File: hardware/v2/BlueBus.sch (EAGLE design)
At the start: 134 parts, among them J1 3PIN_953442_1, J2 6PIN_953442_1, J3 6PIN_5_103166_1, J4 SJ2-35853A-SMT-TR, J5 SMB_CONN, J6 USB3080-30-01-A, J7 PCM12SMTR, J8 TC2030, Q1 NMOSFET-BSS138K, Q2 PMOSFET-DMP32D4SSOT323, Q3 NMOSFET-BSS138K, U1 MPQ4420, U10 PCM5122, U11 PAM8406, U2 TH3122.4, U3 FT231XS, U4 S-1212BC0-U5T1U, U5 XC6210, U6 CAT25M01, U7 PIC24FJ1024GA606, U8 BM83SM1, U9 DIT4096

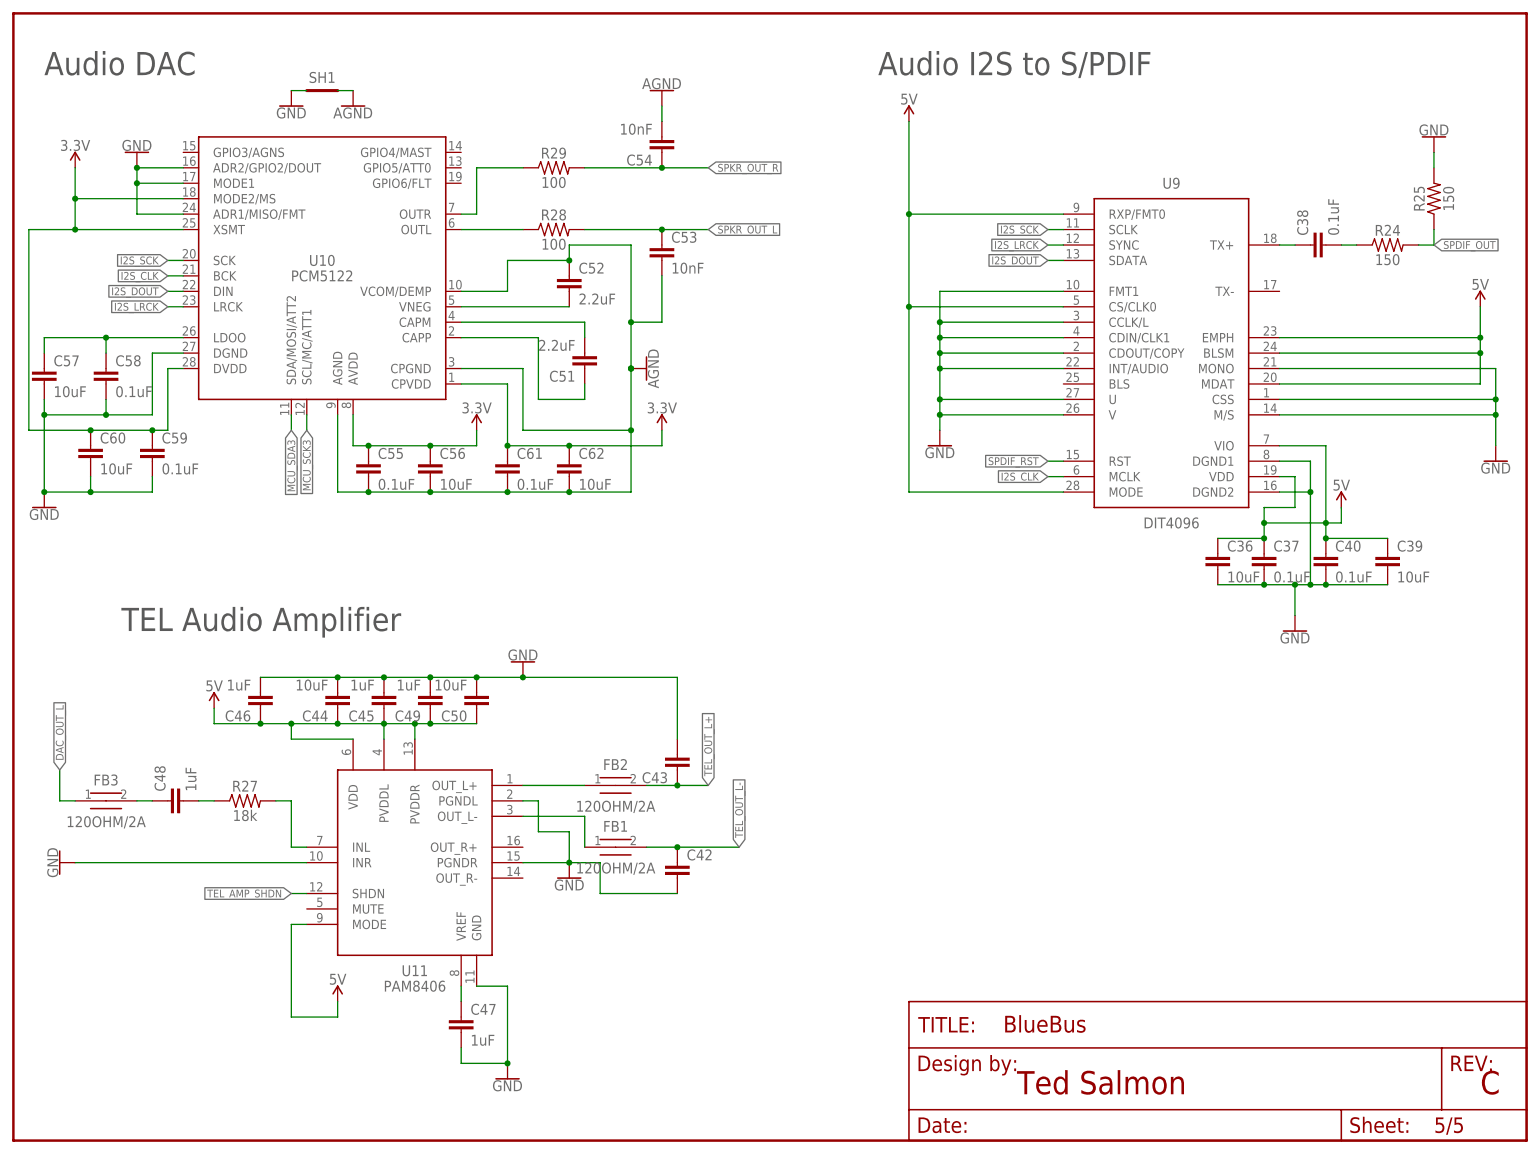
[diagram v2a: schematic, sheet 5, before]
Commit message: [IMP] hardware: V2 Bugfixes and improvements Bug fixes:     * Wire floating S/PDIF reset pin to MCU     * Add pull up to MCU pin 64 for board identification Improvements:     * Added a 0.3mm isolation of the ground plane     * Switched by design rules to metric     * Moved the pin 1 indicators out from under the ICs to the side of pin 1     * Added outlines for all passives     * Moved over the impedance circuit for the S/PDIF output and kept the trace on the top layer     * Moved more traces off the bottom layer     * Moved the I2S lines to the top layer and reduced the VIA count from 11 to 5     * Revised all the packages in the design to ensure they matched the D/S. Specifically, the PIC24s package now has 0.3mm pads     * Set the minimum trace size to 0.25mm instead of 0.20mm     * Added more VIA floods for the ground plane to tie them together where the bottom layer gets bifurcated
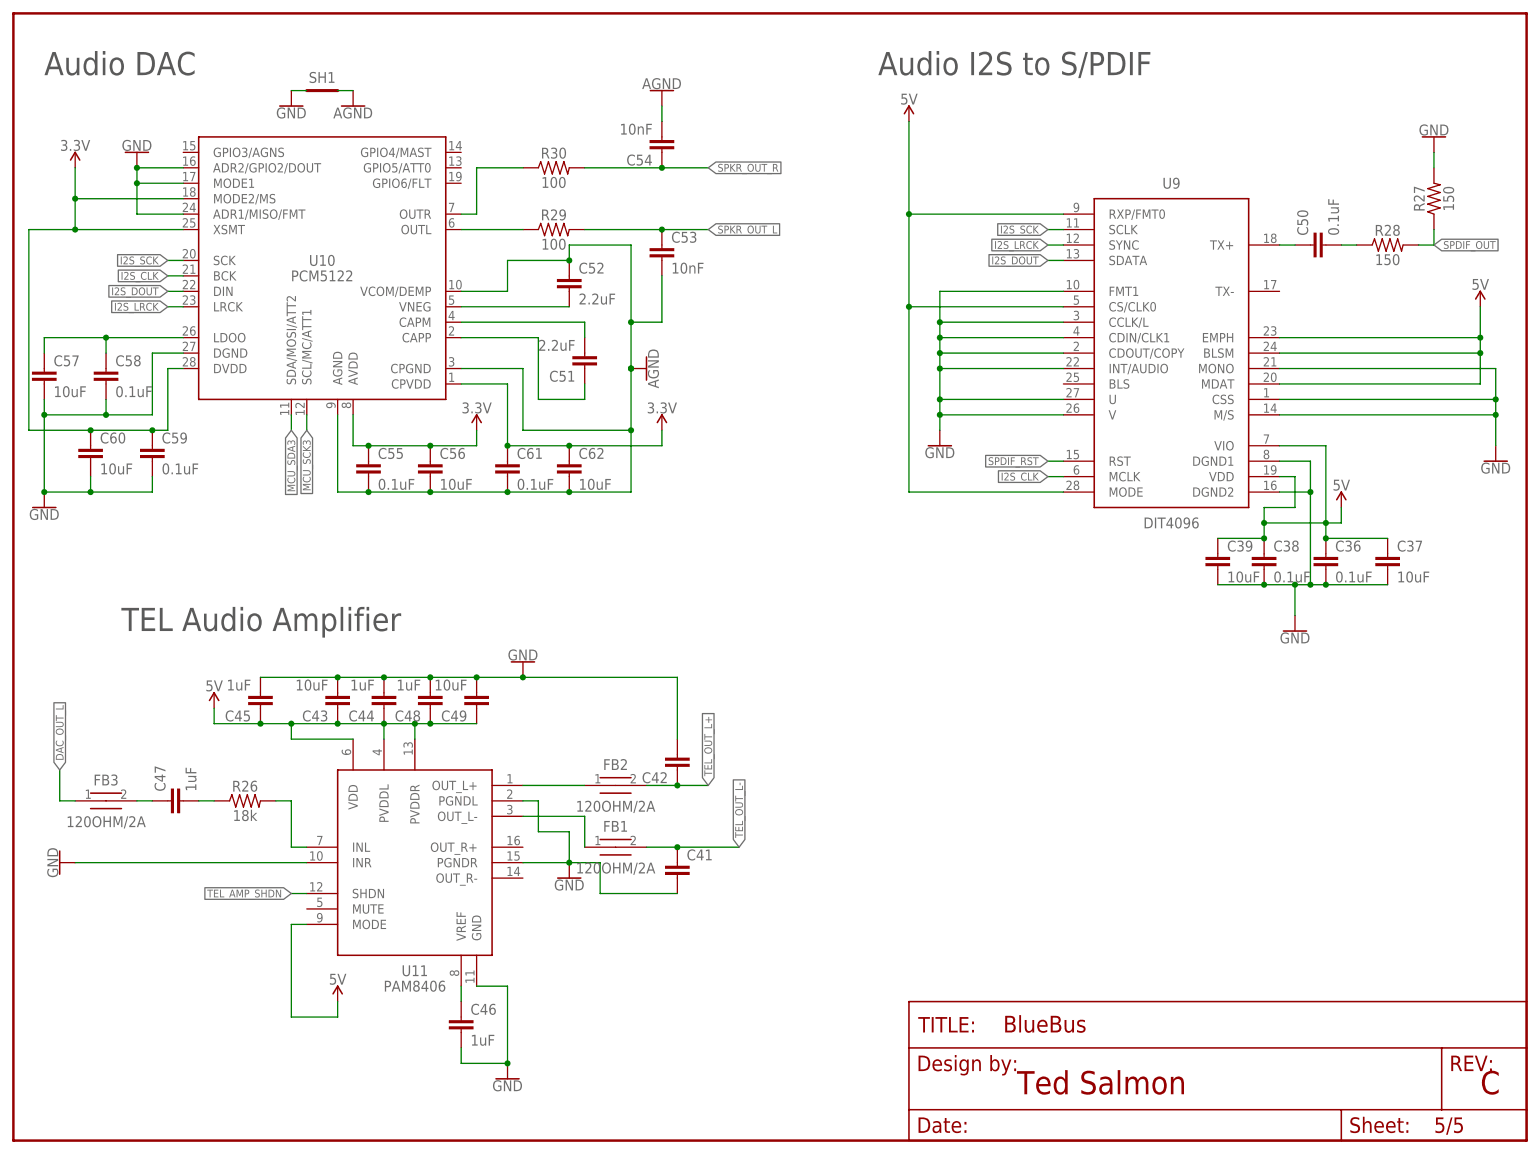
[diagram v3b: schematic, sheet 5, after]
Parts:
- added R30: 100, Passives:100OHM0603
- C31, C32: value 47nF -> 1uF; device Passives:47NF0603 -> Passives:1UF0603
- C33: value 200pF -> 47nF; device Passives:220PF0603 -> Passives:47NF0603
- C34: value 1uF -> 200pF; device Passives:1UF0603 -> Passives:220PF0603
- C35: value 1uF -> 47nF; device Passives:1UF0603 -> Passives:47NF0603
- C36, C50: value 10uF -> 0.1uF; device Passives:10UF0603 -> Passives:0.1UF0603
- C37: value 0.1uF -> 10uF; device Passives:0.1UF0603 -> Passives:10UF0603
- C40: value 0.1uF -> 47UF1206; device Passives:0.1UF0603 -> Passives:47UF1206
- C41: value 47UF1206 -> 200pF; device Passives:47UF1206 -> Passives:220PF0603
- C43: value 200pF -> 10uF; device Passives:220PF0603 -> Passives:10UF0603
- C44: value 10uF -> 1uF; device Passives:10UF0603 -> Passives:1UF0603
- C49: value 1uF -> 10uF; device Passives:1UF0603 -> Passives:10UF0603
- R10: value 20 -> 100k; device Passives:20OHM0603 -> Passives:100KOHM0603
- R17: value 20 -> 10k; device Passives:20OHM0603 -> Passives:10KOHM0603
- R19: value 2k -> 20; device Passives:2KOHM0603 -> Passives:20OHM0603
- R22: value 1k -> 2k; device Passives:1KOHM0603 -> Passives:2KOHM0603
- R24: value 150 -> 1k; device Passives:150OHM0603 -> Passives:1KOHM0603
- R25: value 150 -> 10k; device Passives:150OHM0603 -> Passives:10KOHM0603
- R26: value 10k -> 18k; device Passives:10KOHM0603 -> Passives:18KOHM0603
- R27: value 18k -> 150; device Passives:18KOHM0603 -> Passives:150OHM0603
- R28: value 100 -> 150; device Passives:100OHM0603 -> Passives:150OHM0603
- R5: value 100k -> 20; device Passives:100KOHM0603 -> Passives:20OHM0603
- R6: value 41.2k -> 100k; device Passives:41.2KOHM0603 -> Passives:100KOHM0603
- R7: value 7.68k -> 41.2k; device Passives:7.68KOHM0603 -> Passives:41.2KOHM0603
- R8: value 51k -> 7.68k; device Passives:51KOHM0603 -> Passives:7.68KOHM0603
- R9: value 100k -> 51k; device Passives:100KOHM0603 -> Passives:51KOHM0603
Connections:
- new net MCU_VER: R16.1, U7.HLVDIN/CTED8/PMD4/RE4
- net 12V: now also R25.1; no longer R26.1
- net 3.3V: now also R17.2
- net 5V: now also C38.1, C43.1, C48.1, R7.2; no longer C40.1, C46.1, C50.1, R6.2
- net 5VREG_BS: now also R5.1; no longer R10.1
- net 5VREG_BS_CAP: now also R5.2; no longer R10.2
- net 5VREG_EN: now also R6.1; no longer R5.1
- net 5VREG_FB: now also R9.2; no longer R8.2
- net 5VREG_FB_T: now also R7.1, R8.2, R9.1; no longer R6.1, R7.2, R8.1
- net 5VREG_PG: now also R10.1; no longer R9.1
- net 5VREG_VCC: now also R10.2; no longer R9.2
- net BT_MIC_L: now also C34.1, C40.1; no longer C32.1, C41.1
- net DAC_OUT_L: now also R29.1; no longer R28.1
- net DAC_OUT_R: now also R30.1; no longer R29.1
- net GND: now also C31.2, C32.2, C35.1, C38.2, C41.2, C48.2, R27.2, R8.1; no longer C31.1, C33.2, C35.2, C40.2, C47.2, C50.2, R25.2, R7.1
- net IBUS: now also R19.1; no longer R17.1
- net IBUS_5V: now also R6.2; no longer R5.2
- net IBUS_FILT: now also R19.2; no longer R17.2
- net MCU_ON_LED: now also R20.2; no longer R21.2
- net MCU_ON_LED_RES: now also R20.1; no longer R21.1
- net MCU_SCK3: now also R13.1; no longer R12.1
- net MCU_SDA3: now also R12.1; no longer R13.1
- net MICN1: now also C35.2; no longer C31.2
- net MICP1: now also C33.2; no longer C32.2
- net MICP1_RES: now also C31.1, R24.1; no longer C35.1, R22.1
- net MIC_BIAS: now also C32.1, R24.2; no longer C34.1, R22.2
- net RECOVERY_ON: now also R17.1; no longer R16.1
- net SPDIF_OUT: now also R27.1, R28.2; no longer R24.2, R25.1
- net SPDIF_RST: now also U7.PMD2/RE2
- net SPDIF_TX_FLT: now also C50.1; no longer C38.1
- net SPDIF_TX_RES: now also C50.2, R28.1; no longer C38.2, R24.1
- net SPKR_OUT_L: now also R29.2; no longer R28.2
- net SPKR_OUT_R: now also R30.2; no longer R29.2
- net SYS_RX_LED: now also R21.2; no longer R20.2
- net SYS_RX_LED_RES: now also R21.1; no longer R20.1
- net SYS_TX_LED: now also R22.2; no longer R19.2
- net SYS_TX_LED_RES: now also R22.1; no longer R19.1
- net TEL_AMP_IN: now also C47.1; no longer C48.1
- net TEL_AMP_INL: now also R26.2; no longer R27.2
- net TEL_AMP_INL_CAP_RES: now also C47.2, R26.1; no longer C48.2, R27.1
- net TEL_AMP_VREF: now also C46.1; no longer C47.1
- net TEL_MIC_L_OUT: now also C40.2, R25.2; no longer C41.2, R26.2
- net TEL_OUT_L+: now also C42.1; no longer C43.1
- net TEL_OUT_L-: now also C41.1; no longer C42.1
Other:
- moved on the sheet: C31, C32, C33, C34, C35, C36, C37, C38, C39, C42, C43, C44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

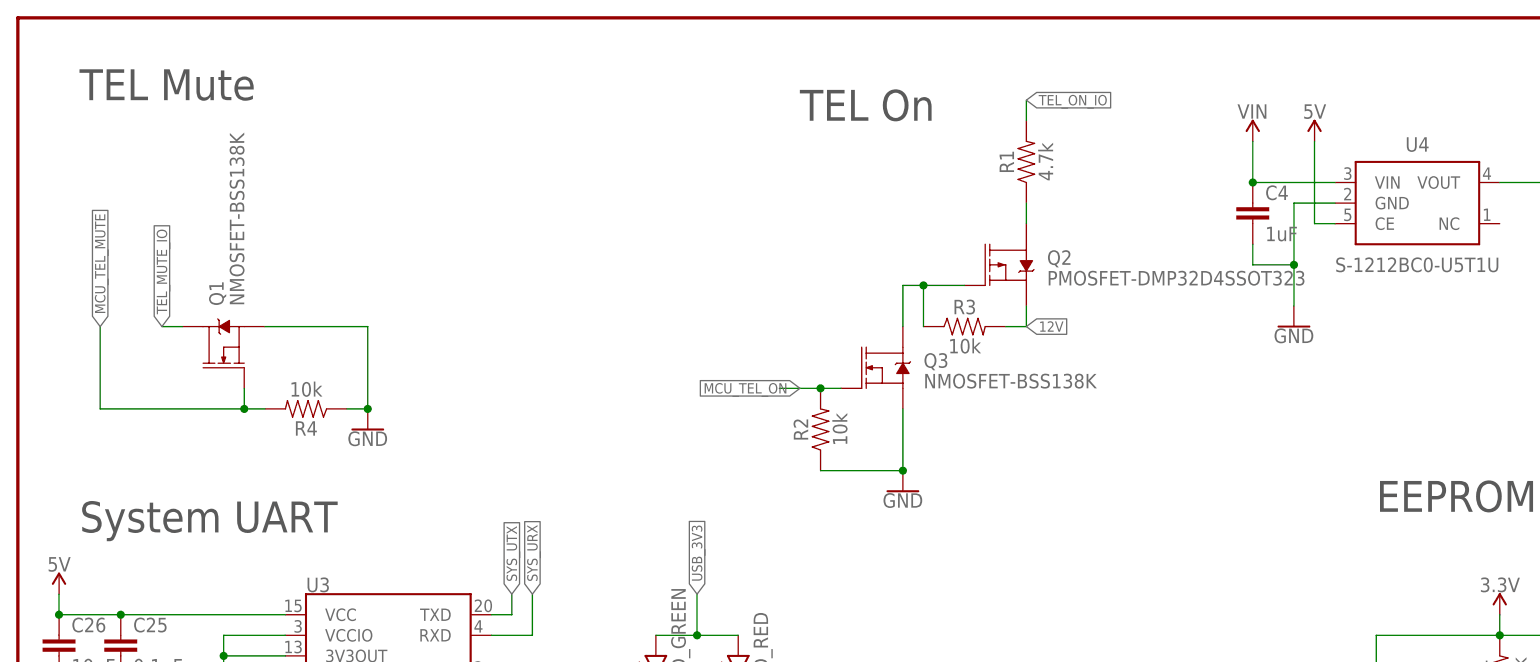
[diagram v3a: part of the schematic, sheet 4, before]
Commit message: [IMP] hardware: v2.0 TEL Circuit * Add Series resistor and move MOSFETs and resistors around to support BJT usage
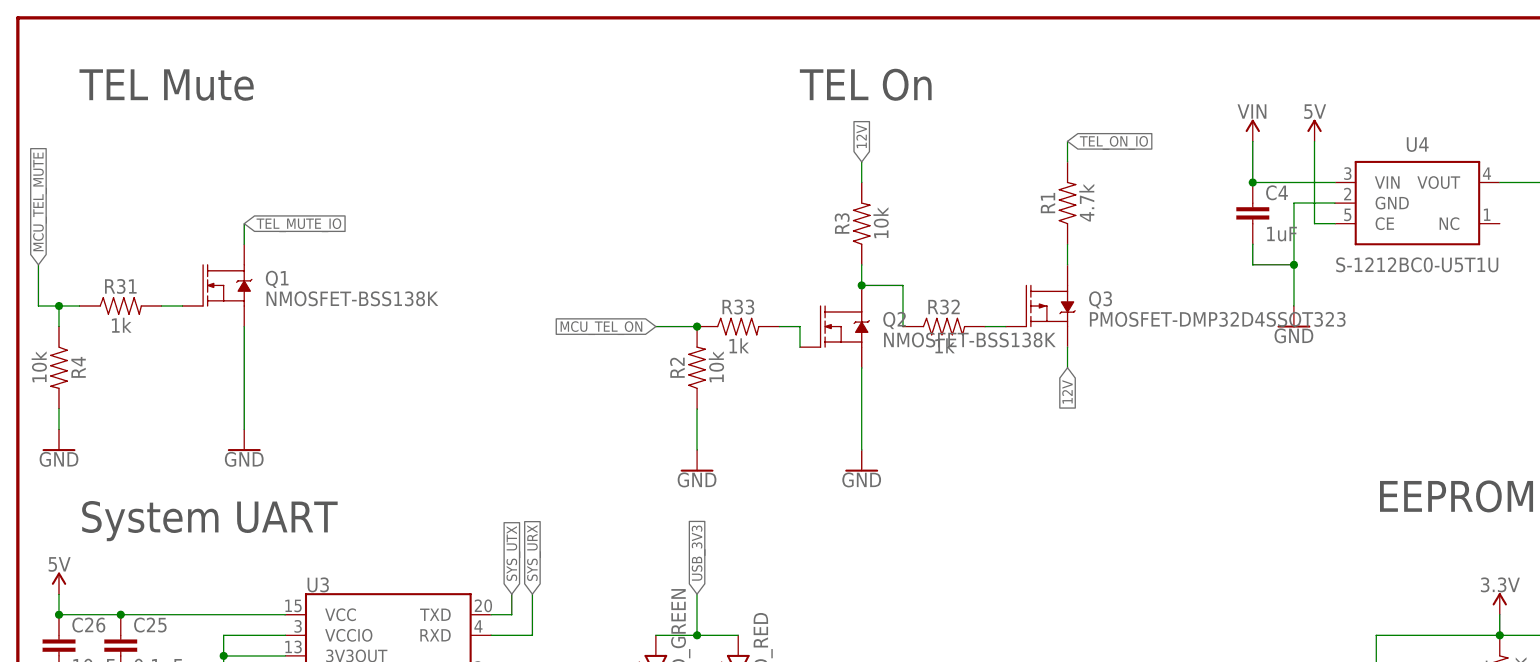
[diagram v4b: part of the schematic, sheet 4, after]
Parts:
- added D3: SMBJ18A, Passives:SMBJ18A
- added R31, R32, R33: 1k, Passives:1KOHM0603
- J8: value TC2030 -> TC2030NL; device Connectors:TC2030 -> Connectors:TC2030NL
- Q2: value PMOSFET-DMP32D4SSOT323 -> NMOSFET-BSS138K; device Passives:PMOSFET-DMP32D4SSOT323 -> Passives:NMOSFET-BSS138K
- Q3: value NMOSFET-BSS138K -> PMOSFET-DMP32D4SSOT323; device Passives:NMOSFET-BSS138K -> Passives:PMOSFET-DMP32D4SSOT323
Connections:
- removed net TEL_ON_EN: Q2.G, Q3.D, R3.1
- new net MCU_TEL_MUTE_RES: Q1.G, R31.2
- new net MCU_TEL_ON_NRES: Q2.G, R33.2
- new net TEL_ON_P: Q2.D, R3.1, R32.1
- new net TEL_ON_P_RES: Q3.G, R32.2
- net 12V: now also Q3.S; no longer Q2.S
- net GND: now also Q2.S, R4.2; no longer Q3.S, R4.1
- net GND_FLT: now also D3.A
- net MCU_TEL_MUTE: now also R31.1, R4.1; no longer Q1.G, R4.2
- net MCU_TEL_ON: now also R33.1; no longer Q3.G
- net TEL_ON: now also Q3.D; no longer Q2.D
- net VBAT_DIODE: now also D3.C
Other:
- moved on the sheet: Q1, Q2, Q3, R1, R2, R3, R4
